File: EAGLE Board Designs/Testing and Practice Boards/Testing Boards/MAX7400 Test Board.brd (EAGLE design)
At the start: 17 x 13.3 mm, 5 parts

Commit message: change silkscreen
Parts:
- U$1: value MAX7400 -> MAX74
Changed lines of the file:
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@@
 <drawing>
 <settings>
-<setting alwaysvectorfont="no"/>
+<setting alwaysvectorfont="yes"/>
 <setting verticaltext="up"/>
 </settings>
@@
 <wire x1="16.871" y1="14.021" x2="-0.127" y2="14.021" width="0" layer="20"/>
 <wire x1="-0.127" y1="14.021" x2="-0.127" y2="0.762" width="0" layer="20"/>
+<polygon width="0.1524" layer="25" spacing="5.08" pour="hatch">
+<vertex x="11.557" y="12.319"/>
+<vertex x="11.557" y="13.589"/>
+<vertex x="13.843" y="13.589"/>
+<vertex x="13.843" y="12.319"/>
+</polygon>
 </plain>
 <attributes>
@@
 </autorouter>
 <elements>
-<element name="C1" library="HyTechDevices" package="0603-CAP" value="750pF" x="10.668" y="6.096" smashed="yes" rot="MR0">
-<attribute name="NAME" x="8.89" y="5.461" size="0.8128" layer="26" font="vector" rot="MR0"/>
-</element>
-<element name="C2" library="HyTechDevices" package="0603-CAP" value="0.1uF" x="10.668" y="4.064" smashed="yes" rot="MR0">
-<attribute name="NAME" x="10.287" y="2.286" size="0.4064" layer="26" font="vector" rot="MR0"/>
-</element>
-<element name="C3" library="HyTechDevices" package="0603-CAP" value="0.1uF" x="5.334" y="10.541" smashed="yes" rot="MR270">
-<attribute name="NAME" x="4.572" y="11.43" size="0.4064" layer="26" font="vector" rot="MR270"/>
-</element>
+<element name="C1" library="HyTechDevices" package="0603-CAP" value="750pF" x="10.668" y="6.096" smashed="yes" rot="MR0"/>
+<element name="C2" library="HyTechDevices" package="0603-CAP" value="0.1uF" x="10.668" y="4.064" smashed="yes" rot="MR0"/>
+<element name="C3" library="HyTechDevices" package="0603-CAP" value="0.1uF" x="5.334" y="10.541" smashed="yes" rot="MR270"/>
 <element name="JP1" library="HyTechDevices" package="1X04" value="" x="2.54" y="7.747" smashed="yes" rot="R90">
 <attribute name="VALUE" x="5.715" y="2.667" size="1.27" layer="27" rot="R90"/>
 </element>
-<element name="U$1" library="HyTechDevices" package="SOP8" value="MAX7400" x="10.541" y="9.652" smashed="yes" rot="MR90">
-<attribute name="VALUE" x="8.636" y="13.589" size="1.27" layer="28" rot="MR180"/>
+<element name="U$1" library="HyTechDevices" package="SOP8" value="MAX74" x="10.541" y="9.652" smashed="yes" rot="MR90">
+<attribute name="VALUE" x="11.176" y="13.589" size="1.27" layer="27" rot="R180"/>
 </element>
 </elements>

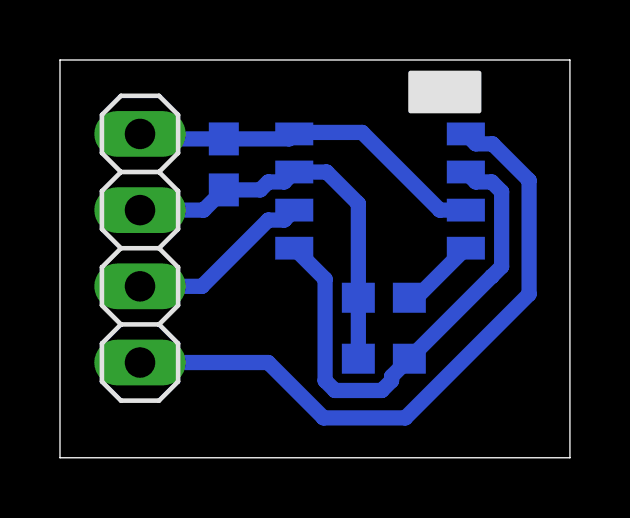
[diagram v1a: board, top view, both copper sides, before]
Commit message: Silkscreen changes
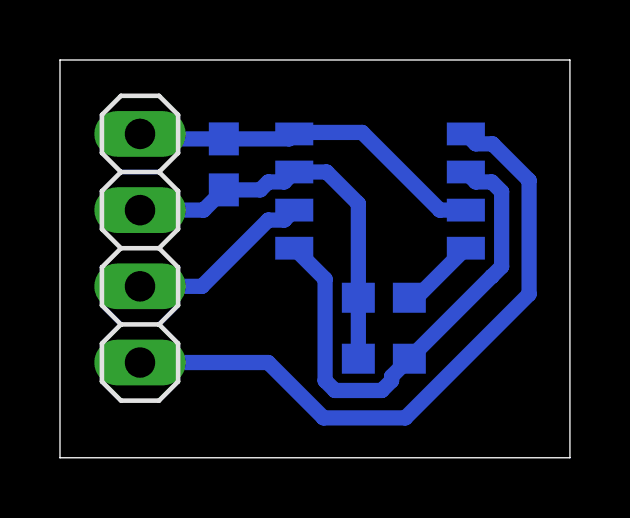
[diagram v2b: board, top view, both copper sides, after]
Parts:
- C3: value 0.1uF -> .1uF
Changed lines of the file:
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@@
 <drawing>
 <settings>
-<setting alwaysvectorfont="yes"/>
+<setting alwaysvectorfont="no"/>
 <setting verticaltext="up"/>
 </settings>
@@
 <wire x1="16.871" y1="14.021" x2="-0.127" y2="14.021" width="0" layer="20"/>
 <wire x1="-0.127" y1="14.021" x2="-0.127" y2="0.762" width="0" layer="20"/>
-<polygon width="0.1524" layer="25" spacing="5.08" pour="hatch">
-<vertex x="11.557" y="12.319"/>
-<vertex x="11.557" y="13.589"/>
-<vertex x="13.843" y="13.589"/>
-<vertex x="13.843" y="12.319"/>
-</polygon>
+<rectangle x1="6.477" y1="12.192" x2="9.017" y2="13.589" layer="28"/>
 </plain>
 <attributes>
@@
 </autorouter>
 <elements>
-<element name="C1" library="HyTechDevices" package="0603-CAP" value="750pF" x="10.668" y="6.096" smashed="yes" rot="MR0"/>
-<element name="C2" library="HyTechDevices" package="0603-CAP" value="0.1uF" x="10.668" y="4.064" smashed="yes" rot="MR0"/>
-<element name="C3" library="HyTechDevices" package="0603-CAP" value="0.1uF" x="5.334" y="10.541" smashed="yes" rot="MR270"/>
+<element name="C1" library="HyTechDevices" package="0603-CAP" value="750pF" x="10.668" y="6.096" smashed="yes" rot="MR0">
+<attribute name="VALUE" x="9.017" y="5.461" size="0.8128" layer="28" font="vector" rot="MR0"/>
+</element>
+<element name="C2" library="HyTechDevices" package="0603-CAP" value="0.1uF" x="10.668" y="4.064" smashed="yes" rot="MR0">
+<attribute name="VALUE" x="9.017" y="3.556" size="0.8128" layer="28" font="vector" rot="MR0"/>
+</element>
+<element name="C3" library="HyTechDevices" package="0603-CAP" value=".1uF" x="5.334" y="10.541" smashed="yes" rot="MR270">
+<attribute name="NAME" x="4.572" y="11.43" size="0.4064" layer="26" font="vector" rot="MR270"/>
+<attribute name="VALUE" x="4.445" y="8.89" size="0.8128" layer="28" font="vector" rot="MR180"/>
+</element>
 <element name="JP1" library="HyTechDevices" package="1X04" value="" x="2.54" y="7.747" smashed="yes" rot="R90">
 <attribute name="VALUE" x="5.715" y="2.667" size="1.27" layer="27" rot="R90"/>
 </element>
 <element name="U$1" library="HyTechDevices" package="SOP8" value="MAX74" x="10.541" y="9.652" smashed="yes" rot="MR90">
-<attribute name="VALUE" x="11.176" y="13.589" size="1.27" layer="27" rot="R180"/>
+<attribute name="VALUE" x="9.144" y="13.589" size="1.27" layer="27" rot="MR180"/>
 </element>
 </elements>
